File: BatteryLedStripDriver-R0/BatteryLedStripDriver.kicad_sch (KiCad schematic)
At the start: 42 parts, among them J1 Screw_Terminal_01x02, J2 Conn_01x03_Male, J3 Screw_Terminal_01x02, J4 Conn_01x02_Male, Q1 2N7002, Q2 DMP2305U, Q3 2N7002, Q4 DMP2305U, Q5 2N7002, SW1 SW_Reed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

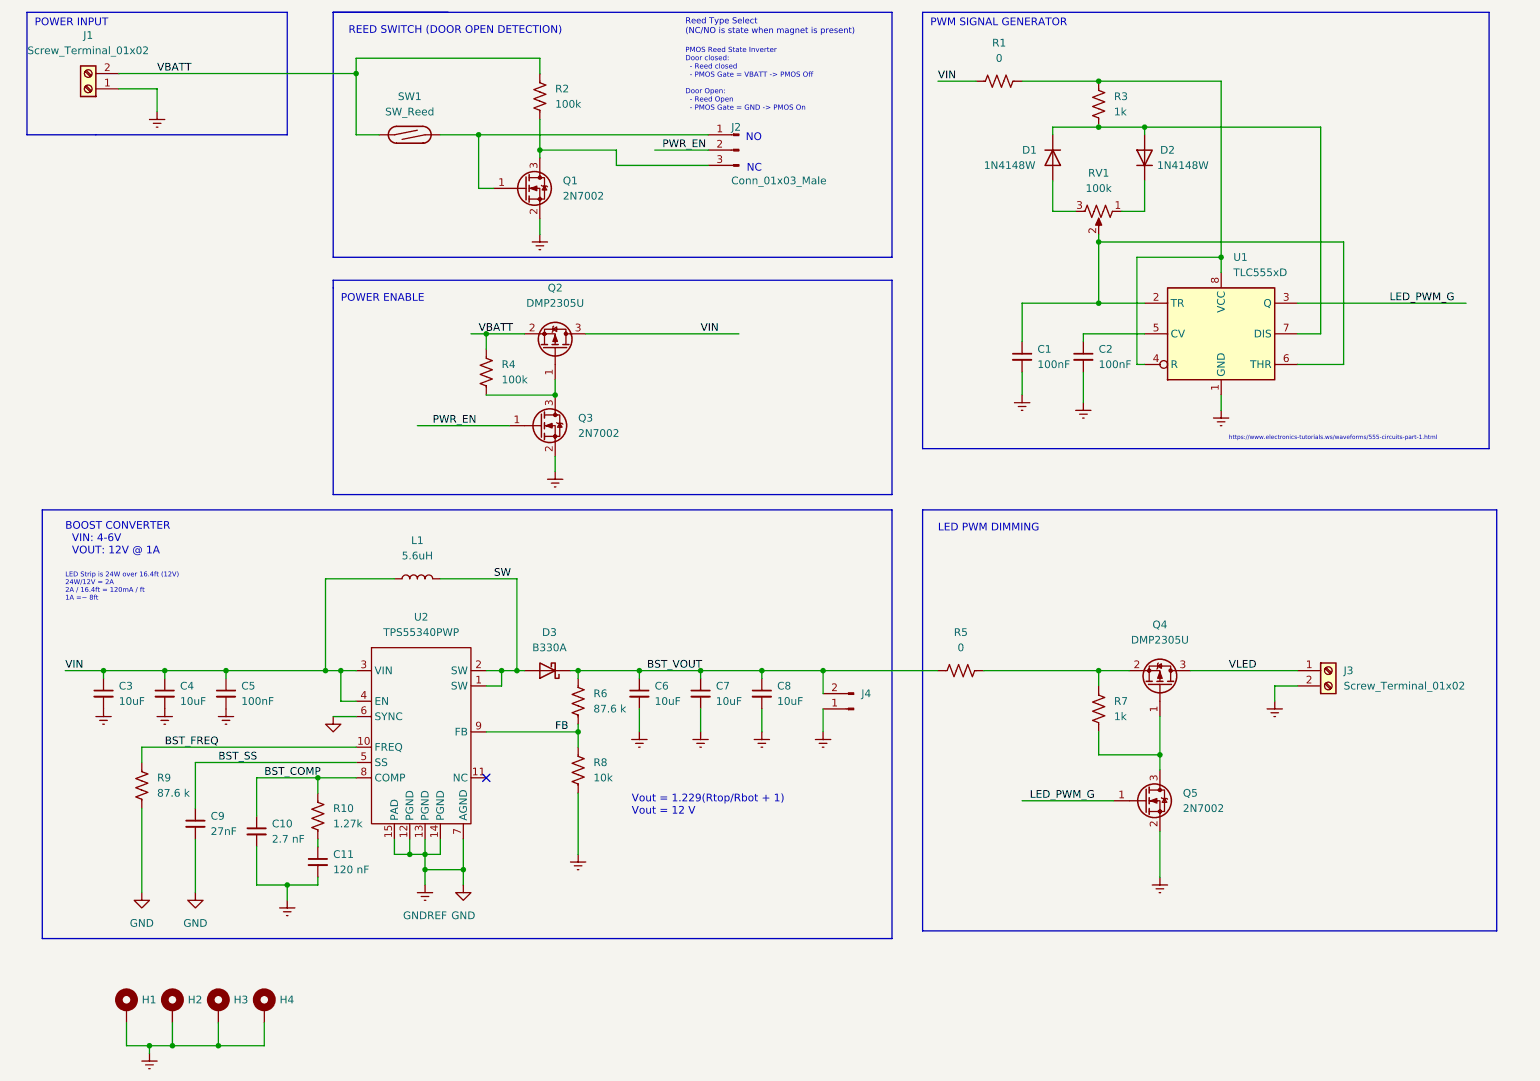
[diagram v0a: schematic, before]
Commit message: fix sch typos, add/update readmes
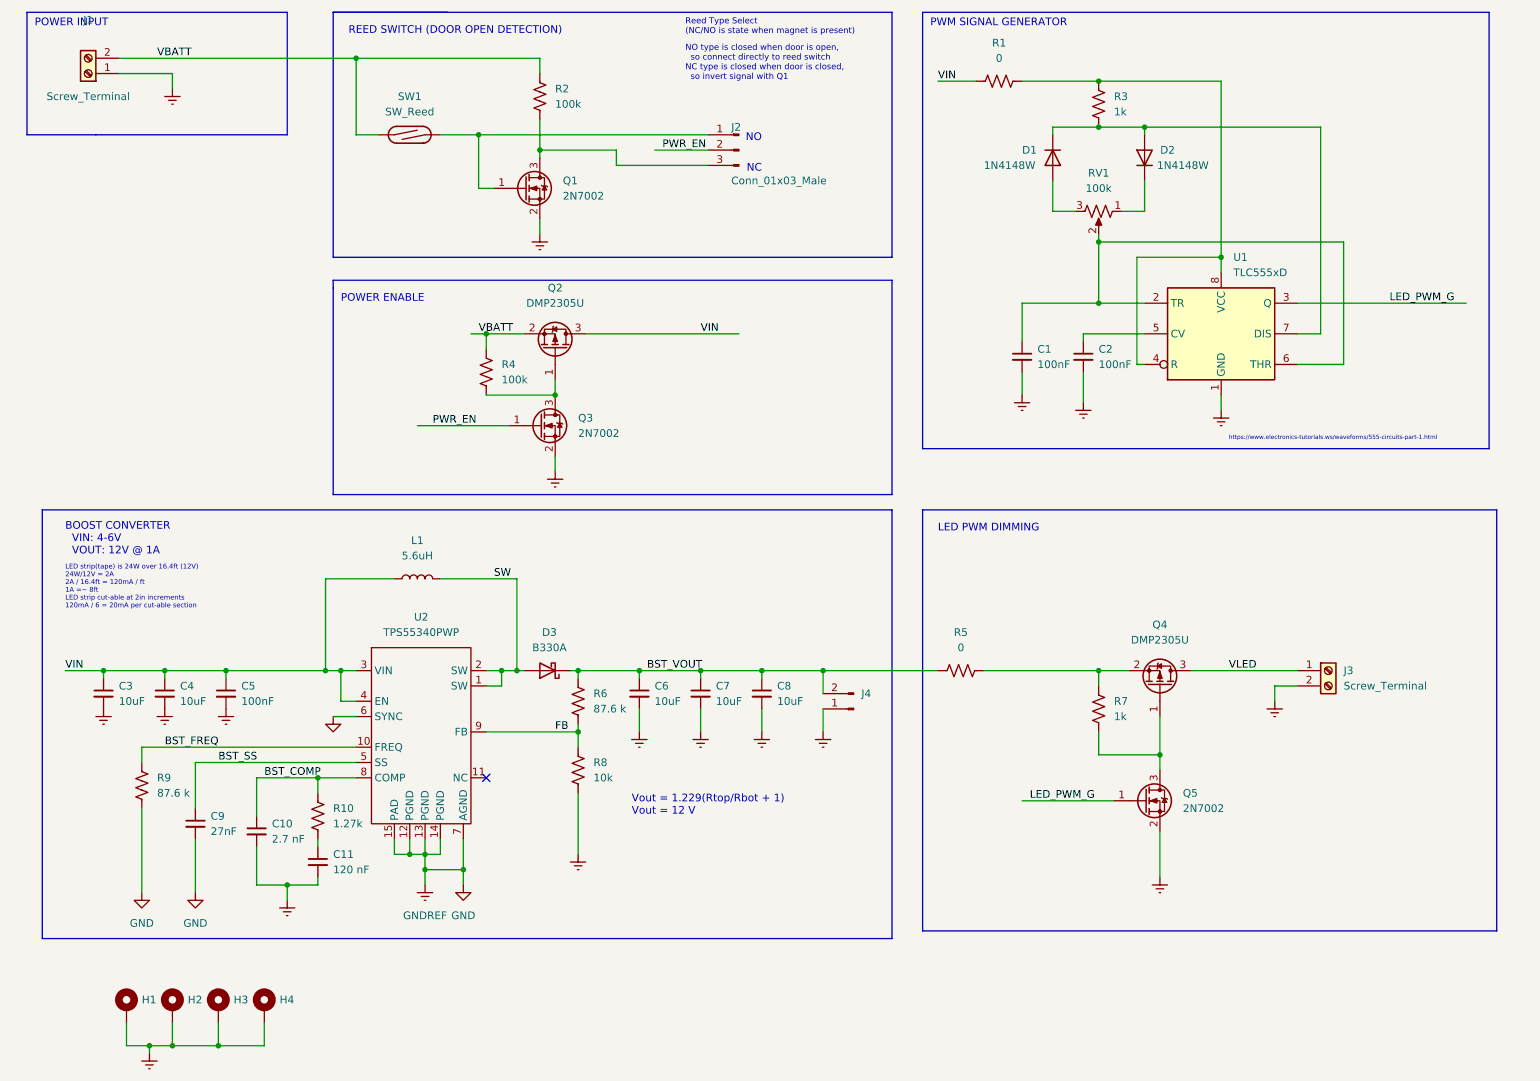
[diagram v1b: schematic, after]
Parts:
- J1, J3: value Screw_Terminal_01x02 -> Screw_Terminal
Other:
- note added: "LED strip(tape) is 24W over 16.4ft (12V) 24W/12V = 2A 2A / 16.4ft = 120mA / ft 1A =~ 8ft LED strip cut-able at 2in increments 120mA / 6 = 20mA per cut-able section"
- note added: "NO type is closed when door is open, so connect directly to reed switch NC type is closed when door is closed, so invert signal with Q1"
- note removed: "LED Strip is 24W over 16.4ft (12V) 24W/12V = 2A 2A / 16.4ft = 120mA / ft 1A =~ 8ft"
- note removed: "PMOS Reed State Inverter Door closed: - Reed closed - PMOS Gate = VBATT -> PMOS Off Door Open: - Reed Open - PMOS Gate = GND -> PMOS On"
- moved on the sheet: J1
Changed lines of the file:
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@@
   (junction (at 68.58 142.24) (diameter 0) (color 0 0 0 0)
   )
-  (junction (at 74.93 25.4) (diameter 0) (color 0 0 0 0)
-  )
   (junction (at 152.4 124.46) (diameter 0) (color 0 0 0 0)
   )
   (junction (at 95.25 35.56) (diameter 0) (color 0 0 0 0)
+  )
+  (junction (at 74.93 22.86) (diameter 0) (color 0 0 0 0)
   )
   (junction (at 107.95 78.74) (diameter 0) (color 0 0 0 0)
@@
     (stroke (width 0) (type default) (color 0 0 0 0))
   )
-  (wire (pts (xy 41.91 27.94) (xy 41.91 31.75))
-    (stroke (width 0) (type default) (color 0 0 0 0))
-  )
   (wire (pts (xy 171.45 26.67) (xy 177.8 26.67))
     (stroke (width 0) (type default) (color 0 0 0 0))
@@
     (stroke (width 0) (type default) (color 0 0 0 0))
   )
+  (wire (pts (xy 44.45 25.4) (xy 44.45 27.94))
+    (stroke (width 0) (type default) (color 0 0 0 0))
+  )
   (wire (pts (xy 105.41 38.1) (xy 105.41 39.37))
     (stroke (width 0) (type default) (color 0 0 0 0))
@@
     (stroke (width 0) (type default) (color 0 0 0 0))
   )
+  (wire (pts (xy 35.56 25.4) (xy 44.45 25.4))
+    (stroke (width 0) (type default) (color 0 0 0 0))
+  )
   (wire (pts (xy 234.95 68.58) (xy 234.95 34.29))
     (stroke (width 0) (type default) (color 0 0 0 0))
@@
     (stroke (width 0) (type default) (color 0 0 0 0))
   )
-  (wire (pts (xy 74.93 25.4) (xy 74.93 35.56))
+  (wire (pts (xy 74.93 22.86) (xy 74.93 35.56))
     (stroke (width 0) (type default) (color 0 0 0 0))
   )
@@
     (stroke (width 0) (type default) (color 0 0 0 0))
   )
-  (wire (pts (xy 35.56 25.4) (xy 74.93 25.4))
+  (wire (pts (xy 35.56 22.86) (xy 74.93 22.86))
     (stroke (width 0) (type default) (color 0 0 0 0))
   )
@@
     (stroke (width 0) (type default) (color 0 0 0 0))
   )
-  (wire (pts (xy 74.93 22.86) (xy 74.93 25.4))
-    (stroke (width 0) (type default) (color 0 0 0 0))
-  )
   (wire (pts (xy 208.28 138.43) (xy 208.28 132.08))
     (stroke (width 0) (type default) (color 0 0 0 0))
@@
   )
   (wire (pts (xy 198.12 53.34) (xy 198.12 63.5))
-    (stroke (width 0) (type default) (color 0 0 0 0))
-  )
-  (wire (pts (xy 35.56 27.94) (xy 41.91 27.94))
     (stroke (width 0) (type default) (color 0 0 0 0))
   )
@@
     (effects (font (size 0.7 0.7)) (justify left bottom))
   )
-  (text "LED Strip is 24W over 16.4ft (12V)\n24W/12V = 2A \n2A / 16.4ft = 120mA / ft\n1A =~ 8ft "
-    (at 26.67 113.03 0)
+  (text "NO type is closed when door is open, \n  so connect directly to reed switch\nNC type is closed when door is closed, \n  so invert signal with Q1"
+    (at 129.54 26.67 0)
+    (effects (font (size 1 1)) (justify left bottom))
+  )
+  (text "LED strip(tape) is 24W over 16.4ft (12V)\n24W/12V = 2A \n2A / 16.4ft = 120mA / ft \n1A =~ 8ft \nLED strip cut-able at 2in increments\n120mA / 6 = 20mA per cut-able section"
+    (at 26.67 114.3 0)
     (effects (font (size 0.8 0.8)) (justify left bottom))
   )
@@
   (text "BOOST CONVERTER\n  VIN: 4-6V\n  VOUT: 12V @ 1A" (at 26.67 105.41 0)
     (effects (font (size 1.27 1.27)) (justify left bottom))
-  )
-  (text "PMOS Reed State Inverter\nDoor closed:\n  - Reed closed\n  - PMOS Gate = VBATT -> PMOS Off\n\nDoor Open:\n  - Reed Open\n  - PMOS Gate = GND -> PMOS On"
-    (at 129.54 31.75 0)
-    (effects (font (size 0.85 0.85)) (justify left bottom))
   )
   (text "NC" (at 142.24 41.91 180)
@@
     (effects (font (size 1.27 1.27)) (justify left bottom))
   )
-  (label "VBATT" (at 41.91 25.4 0)
+  (label "VBATT" (at 41.91 22.86 0)
     (effects (font (size 1.27 1.27)) (justify left bottom))
   )
@@
     (pin "3")
   )
-  (symbol (lib_id "Connector:Screw_Terminal_01x02") (at 30.48 27.94 180) (unit 1)
-    (in_bom yes) (on_board yes) (fields_autoplaced)
-    (property "Reference" "J1" (id 0) (at 30.48 19.05 0))
-    (property "Value" "Screw_Terminal_01x02" (id 1) (at 30.48 21.59 0))
-    (property "Footprint" "TerminalBlock_Phoenix:TerminalBlock_Phoenix_MKDS-1,5-2_1x02_P5.00mm_Horizontal" (id 2) (at 30.48 27.94 0)
-      (effects (font (size 1.27 1.27)) hide)
-    )
-    (property "Datasheet" "~" (id 3) (at 30.48 27.94 0)
-      (effects (font (size 1.27 1.27)) hide)
-    )
-    (property "LCSC Part #" "C474881" (id 4) (at 30.48 27.94 0)
+  (symbol (lib_id "Connector:Screw_Terminal_01x02") (at 30.48 25.4 180) (unit 1)
+    (in_bom yes) (on_board yes)
+    (property "Reference" "J1" (id 0) (at 30.48 16.51 0))
+    (property "Value" "Screw_Terminal" (id 1) (at 30.48 29.21 0))
+    (property "Footprint" "TerminalBlock_Phoenix:TerminalBlock_Phoenix_MKDS-1,5-2_1x02_P5.00mm_Horizontal" (id 2) (at 30.48 25.4 0)
+      (effects (font (size 1.27 1.27)) hide)
+    )
+    (property "Datasheet" "~" (id 3) (at 30.48 25.4 0)
+      (effects (font (size 1.27 1.27)) hide)
+    )
+    (property "LCSC Part #" "C474881" (id 4) (at 30.48 25.4 0)
       (effects (font (size 1.27 1.27)) hide)
     )
@@
       (effects (font (size 1.27 1.27)) (justify left))
     )
-    (property "Value" "Screw_Terminal_01x02" (id 1) (at 238.76 126.9999 0)
+    (property "Value" "Screw_Terminal" (id 1) (at 238.76 126.9999 0)
       (effects (font (size 1.27 1.27)) (justify left))
     )
@@
     (pin "1")
   )
-  (symbol (lib_id "power:GNDREF") (at 41.91 31.75 0) (unit 1)
-    (in_bom yes) (on_board yes) (fields_autoplaced)
-    (property "Reference" "#PWR01" (id 0) (at 41.91 38.1 0)
-      (effects (font (size 1.27 1.27)) hide)
-    )
-    (property "Value" "GNDREF" (id 1) (at 41.91 36.83 0)
-      (effects (font (size 1.27 1.27)) hide)
-    )
-    (property "Footprint" "" (id 2) (at 41.91 31.75 0)
-      (effects (font (size 1.27 1.27)) hide)
-    )
-    (property "Datasheet" "" (id 3) (at 41.91 31.75 0)
+  (symbol (lib_id "power:GNDREF") (at 44.45 27.94 0) (unit 1)
+    (in_bom yes) (on_board yes) (fields_autoplaced)
+    (property "Reference" "#PWR01" (id 0) (at 44.45 34.29 0)
+      (effects (font (size 1.27 1.27)) hide)
+    )
+    (property "Value" "GNDREF" (id 1) (at 44.45 33.02 0)
+      (effects (font (size 1.27 1.27)) hide)
+    )
+    (property "Footprint" "" (id 2) (at 44.45 27.94 0)
+      (effects (font (size 1.27 1.27)) hide)
+    )
+    (property "Datasheet" "" (id 3) (at 44.45 27.94 0)
       (effects (font (size 1.27 1.27)) hide)
     )
@@
     )
     (path "/132f0ed9-d441-409f-9e6f-dcbdc0b11729"
-      (reference "J1") (unit 1) (value "Screw_Terminal_01x02") (footprint "TerminalBlock_Phoenix:TerminalBlock_Phoenix_MKDS-1,5-2_1x02_P5.00mm_Horizontal")
+      (reference "J1") (unit 1) (value "Screw_Terminal") (footprint "TerminalBlock_Phoenix:TerminalBlock_Phoenix_MKDS-1,5-2_1x02_P5.00mm_Horizontal")
     )
     (path "/d3551c38-5149-4a7c-a32e-42dce29d8d0d"
@@
     )
     (path "/409f20d8-aaf7-4be3-8de9-13a4a2237902"
-      (reference "J3") (unit 1) (value "Screw_Terminal_01x02") (footprint "TerminalBlock_Phoenix:TerminalBlock_Phoenix_MKDS-1,5-2_1x02_P5.00mm_Horizontal")
+      (reference "J3") (unit 1) (value "Screw_Terminal") (footprint "TerminalBlock_Phoenix:TerminalBlock_Phoenix_MKDS-1,5-2_1x02_P5.00mm_Horizontal")
     )
     (path "/042f5c24-c44c-4c93-a1ec-f4dbef7cff1b"
